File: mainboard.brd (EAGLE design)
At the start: 85.7 x 54 mm, 136 parts, among them X1 FH12-24S-0.5SH

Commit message: Finished rev 3 schematic and component placement
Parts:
- added C18, C19: (no value), rcl:C0603
- added LED2: (no value), eagle-ltspice:LED_SML0603
- added R12: (no value), resistor:R0402
- moved R11 32.1 mm to (2.11, 47.6), turned to 0 degrees
- moved LED1 28.1 mm to (2.06, 47.7), flipped to the top, turned to 180 degrees
- flipped TP7 to the bottom
- flipped TP8 to the bottom
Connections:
- new net N$60: LED2.A, R12.2
- net +3V3: now also C18.2, R12.1
- net GND: now also C18.1, C19.1, LED2.C
- net VCC/2: now also C19.2
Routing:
- net GND: track 312.4 -> 0.00 mm, vias 25 -> 0
- net +3V3: track 245.3 -> 0.00 mm, vias 10 -> 0
- net KEYROW3: track 142.1 -> 0.00 mm, vias 3 -> 0
- net KEYROW1: track 137.5 -> 0.00 mm, vias 3 -> 0
- net SD_DAT1: track 109.4 -> 0.00 mm
- net SD_DAT3: track 109.0 -> 0.00 mm, vias 2 -> 0
- net SD_DAT0: track 107.5 -> 0.00 mm, vias 2 -> 0
- net KEYROW2: track 106.7 -> 0.00 mm, vias 1 -> 0
- net KEYCOL7: track 103.5 -> 0.00 mm, vias 4 -> 0
- net KEYROW0: track 102.4 -> 0.00 mm, vias 2 -> 0
- net SD_SWITCH: track 100.6 -> 0.00 mm, vias 2 -> 0
- net V+: track 98.0 -> 0.00 mm, vias 2 -> 0
- net KEYCOL9: track 94.5 -> 0.00 mm, vias 6 -> 0
- net KEYCOL8: track 88.7 -> 0.00 mm, vias 5 -> 0
- net KEYCOL10: track 88.1 -> 0.00 mm, vias 3 -> 0
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
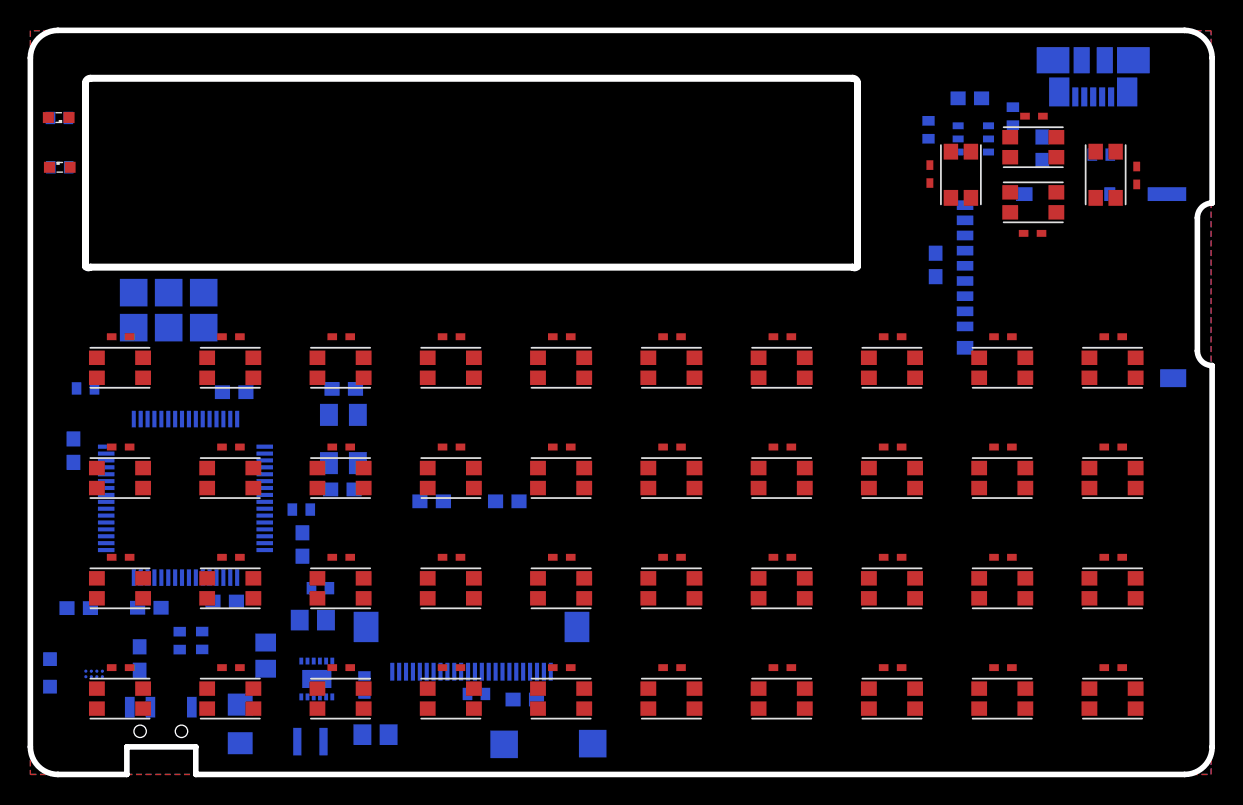
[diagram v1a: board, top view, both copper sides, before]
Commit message: Finished Rev 6 pcb routing
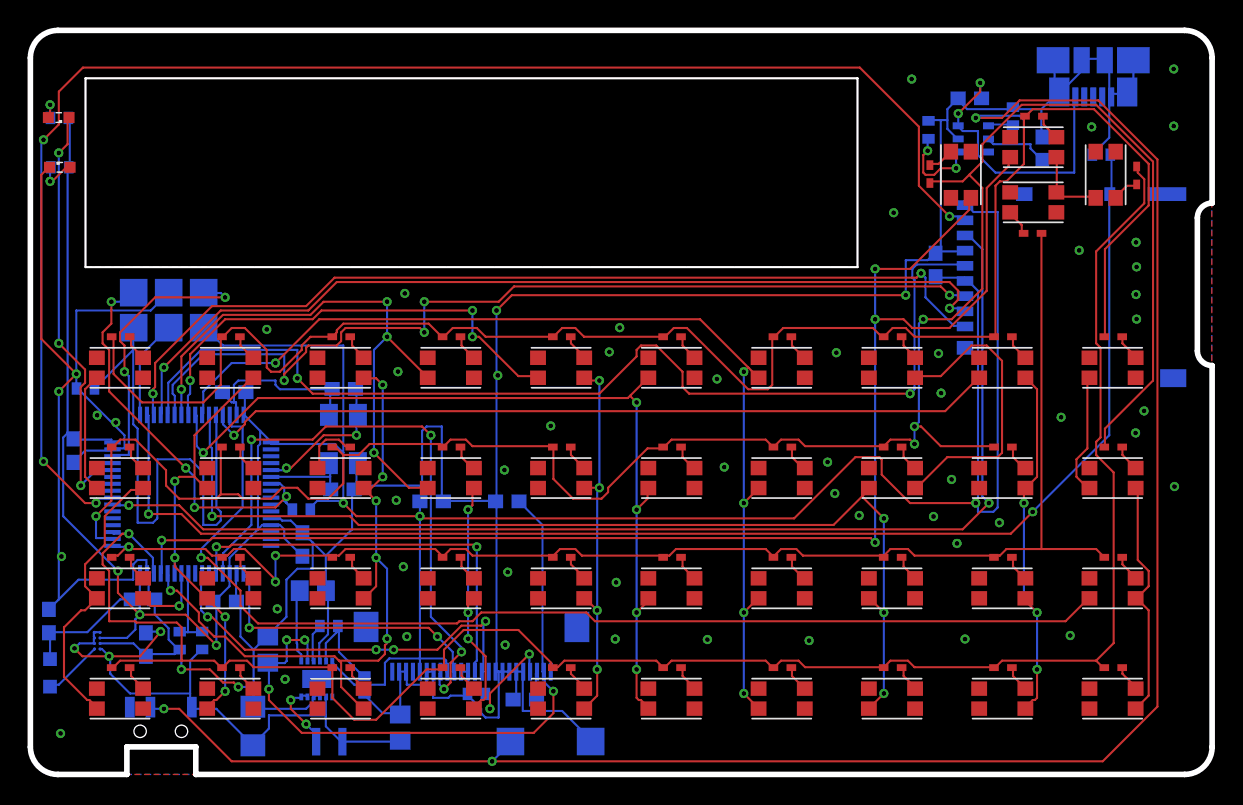
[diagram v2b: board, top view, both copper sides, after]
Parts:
- moved R1 2.81 mm to (21.7, 10.8)
- moved U$6 2.42 mm to (4.85, 9.70), turned to 0 degrees
- moved C12 2.35 mm to (1.35, 11.1), turned to 90 degrees
- moved C3 2.13 mm to (20.5, 13.3)
- moved C1 1.86 mm to (26.8, 3.40), turned to 90 degrees
- moved U$5 1.37 mm to (21.7, 2.38)
- moved C11 1.11 mm to (8.38, 9.42), turned to 270 degrees
- moved C17 0.93 mm to (16.1, 3.51)
- moved C6 0.76 mm to (8.17, 12.7)
- moved U$1 0.55 mm to (11.7, 20.3)
- moved TP7 0.50 mm to (34.8, 2.39)
- moved C2 0.47 mm to (17.2, 9.06), turned to 90 degrees
- moved TP8 0.22 mm to (40.6, 2.39)
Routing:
- net GND: track 0.00 -> 312.1 mm, vias 0 -> 57
- net +3V3: track 0.00 -> 243.0 mm, vias 0 -> 6
- net KEYROW1: track 0.00 -> 156.6 mm, vias 0 -> 4
- net V+: track 0.00 -> 143.8 mm, vias 0 -> 3
- net KEYROW3: track 0.00 -> 141.7 mm, vias 0 -> 1
- net KEYROW0: track 0.00 -> 125.8 mm
- net KEYCOL10: track 0.00 -> 109.4 mm, vias 0 -> 4
- net SD_DAT1: track 0.00 -> 107.7 mm, vias 0 -> 4
- net KEYCOL9: track 0.00 -> 107.3 mm, vias 0 -> 1
- net KEYROW2: track 0.00 -> 103.9 mm, vias 0 -> 3
- net SD_SWITCH: track 0.00 -> 101.0 mm, vias 0 -> 2
- net KEYCOL7: track 0.00 -> 96.3 mm, vias 0 -> 4
- net SD_DAT0: track 0.00 -> 85.5 mm, vias 0 -> 2
- net KEYCOL8: track 0.00 -> 84.7 mm, vias 0 -> 4
- net SD_CLK: track 0.00 -> 76.8 mm, vias 0 -> 2
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- added copper zone on layer 1, net N$62
- added copper zone on layer 16, net N$63
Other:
- outline, holes or cut-outs redrawn
